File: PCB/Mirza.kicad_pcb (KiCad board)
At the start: 2 copper layers, 74 x 34 mm, 95 parts, among them J1 In, J2 Out, J3 Power, Q1 BCM857DS, Q10 BCM857DS, Q11 BCM847DS, Q12 BCM847DS, Q13 2SC3324, Q14 2SA1312, Q15 2SA1312, Q16 2SA1312, Q17 2SC3324, Q18 2SC3324, Q19 2SC3324, Q2 BCM847DS, Q20 2SA1312, Q21 BCM857DS, Q22 BCM847DS, Q23 2SA1312, Q24 2SC3324, Q25 2SC3324, Q26 2SA1312, Q27 D45H11, Q28 D44H11, Q3 2SA1312, Q4 2SC3324, Q5 2SC3324, Q6 2SC3324, Q7 2SA1312, Q8 2SA1312, Q9 BCM857DS, U1 ADA4522-1

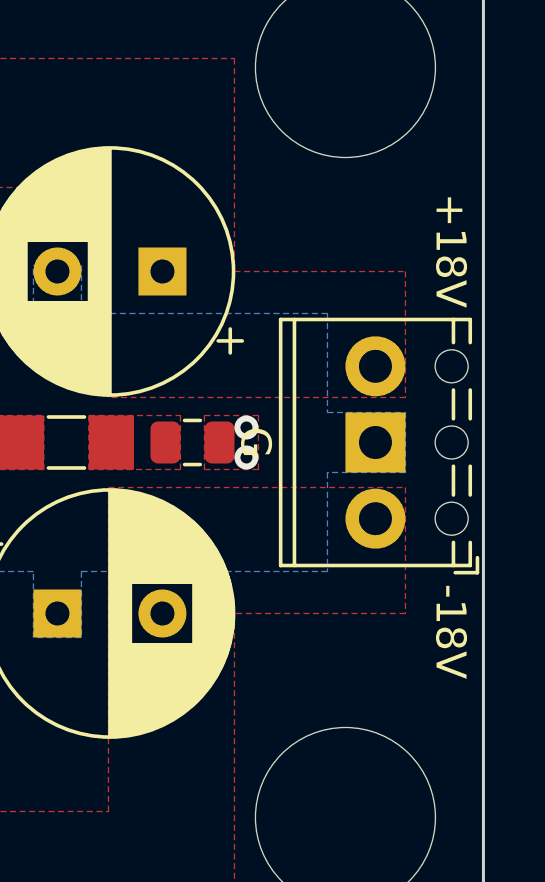
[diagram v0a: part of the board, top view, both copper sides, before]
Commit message: 05/10/2023 update
Changed input voltage to 15V.
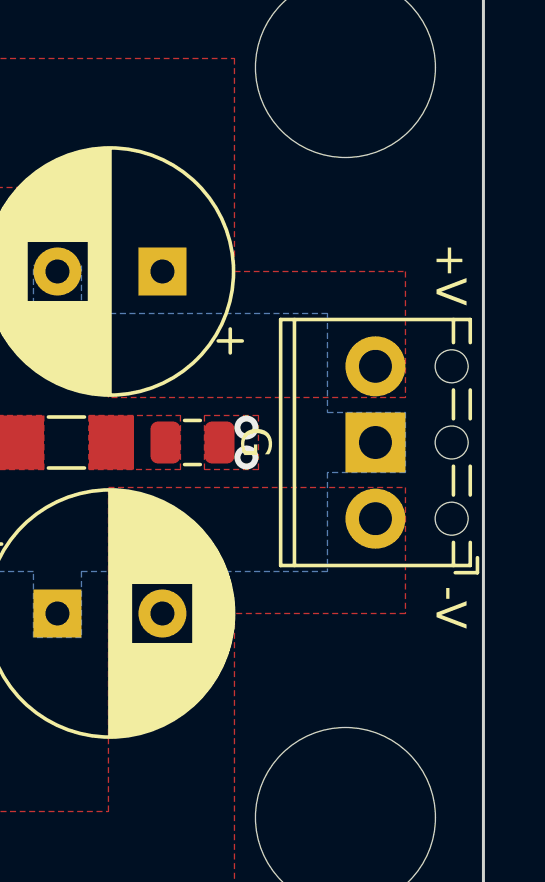
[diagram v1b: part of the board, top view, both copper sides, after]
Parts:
- removed R41: 100k, Resistor_SMD:R_MiniMELF_MMA-0204
- added R33: 10k, Resistor_SMD:R_MiniMELF_MMA-0204, F.Cu at (77.1, 63.4)
- R11, R14: value 150 -> 68
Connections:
- net +18V renamed +15V
- net -18V renamed -15V
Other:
- board text added: "+V"
- board text added: "-V"
- board text removed: "+18V"
- board text removed: "-18V"
